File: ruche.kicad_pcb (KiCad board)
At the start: 2 copper layers, 71.8 x 99.9 mm, 92 parts, among them IC1 CN3791, IC2 MAX17048G+, IC3 L86-M33, IC4 SHT41-AD1B-R3, IC5 HX711, J1 Conn_01x02, J13 Micro_SD_Card, J14 Conn_01x03, J15 Conn_01x05, J3 Conn_01x03, J5 Conn_01x04, J6 Conn_01x02, J7 Conn_01x02, J8 Conn_01x03, J9 Conn_01x03, Q1 AO3401A, Q2 MMBT4403, U1 MKRWAN_1310, U2 MS5611-01BA, U3 XC6220B331MR

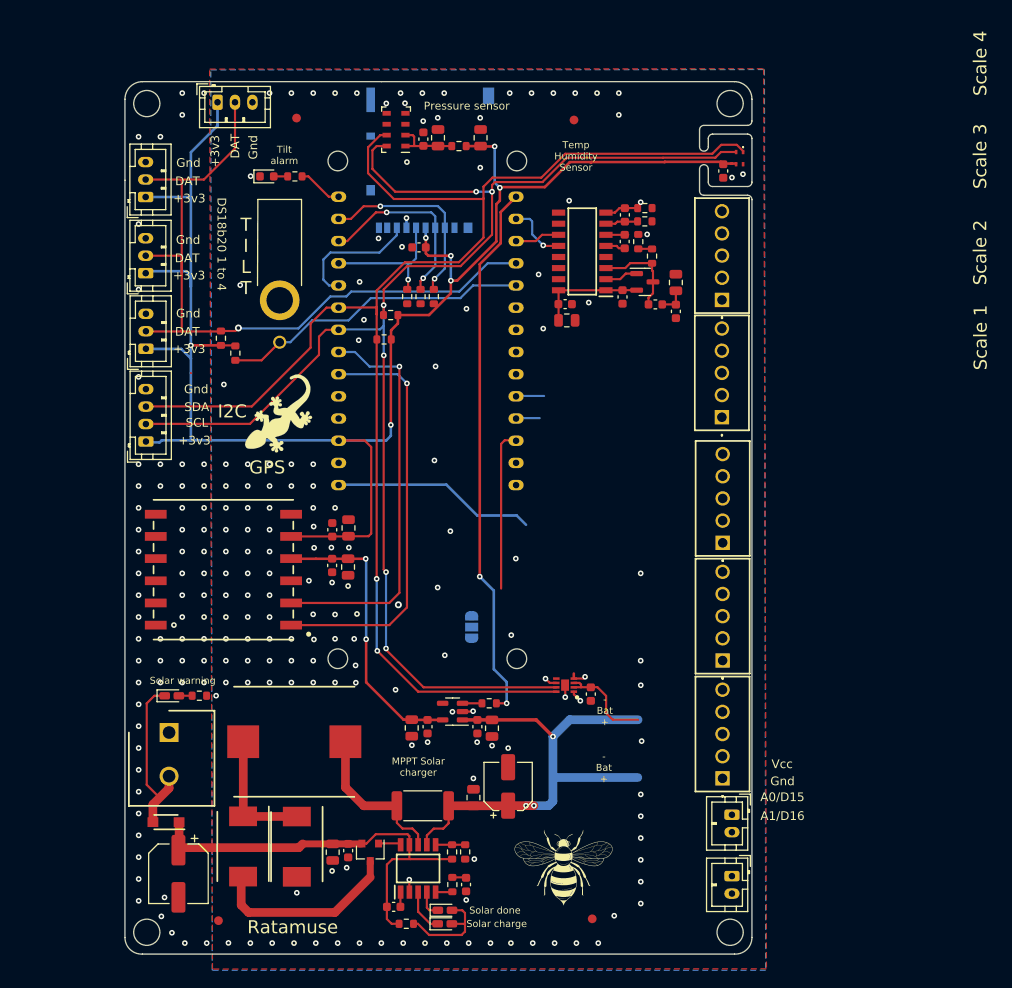
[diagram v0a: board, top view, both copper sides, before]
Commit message: Added HX711
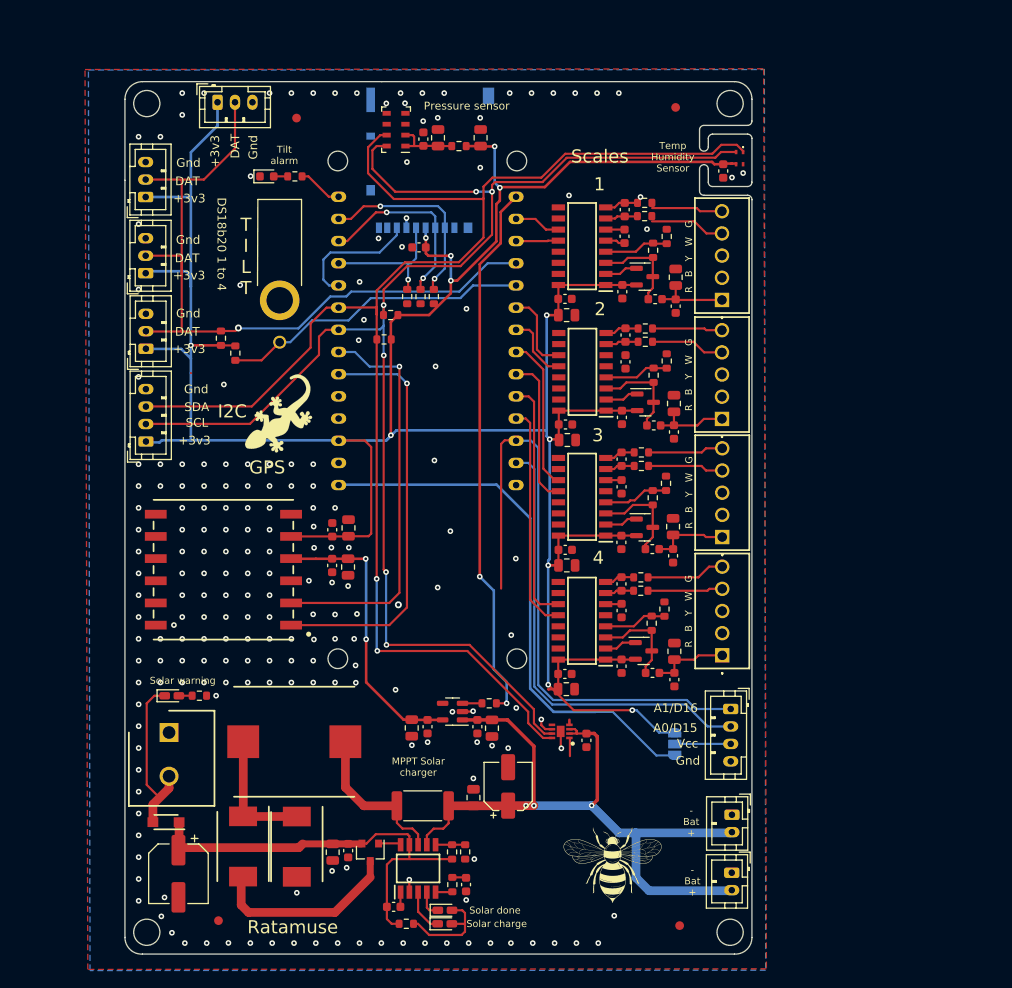
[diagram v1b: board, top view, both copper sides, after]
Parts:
- removed the J15 at (164.9, 148.9)
- removed the J15 at (164.9, 107.5)
- removed the J15 at (164.9, 135.4)
- removed the J15 at (164.9, 121.9)
- added C29: 0.1µF, Capacitor_SMD:C_0603_1608Metric, F.Cu at (159.4, 109.2)
- added C30: 10µF, Capacitor_SMD:C_0805_2012Metric, F.Cu at (159.4, 106.0)
- added C31: 0.1µF, Capacitor_SMD:C_0603_1608Metric, F.Cu at (153.8, 98.1)
- added C32: 0.1µF, Capacitor_SMD:C_0603_1608Metric, F.Cu at (153.8, 101.2)
- added C33: 0.1µF, Capacitor_SMD:C_0603_1608Metric, F.Cu at (153.4, 107.5)
- added C34: 0.1µF, Capacitor_SMD:C_0603_1608Metric, F.Cu at (146.9, 108.4)
- added C35: 10µF, Capacitor_SMD:C_0805_2012Metric, F.Cu at (147.2, 110.1)
- added C36: 0.1µF, Capacitor_SMD:C_0603_1608Metric, F.Cu at (159.3, 123.4)
- added C37: 10µF, Capacitor_SMD:C_0805_2012Metric, F.Cu at (159.3, 120.1)
- added C38: 0.1µF, Capacitor_SMD:C_0603_1608Metric, F.Cu at (153.4, 112.3)
- added C39: 0.1µF, Capacitor_SMD:C_0603_1608Metric, F.Cu at (153.4, 115.5)
- added C40: 0.1µF, Capacitor_SMD:C_0603_1608Metric, F.Cu at (153.3, 121.9)
- added C41: 0.1µF, Capacitor_SMD:C_0603_1608Metric, F.Cu at (146.9, 122.7)
- added C42: 10µF, Capacitor_SMD:C_0805_2012Metric, F.Cu at (147.1, 124.5)
- added C43: 0.1µF, Capacitor_SMD:C_0603_1608Metric, F.Cu at (159.4, 137.6)
- added C44: 10µF, Capacitor_SMD:C_0805_2012Metric, F.Cu at (159.4, 134.3)
- added C45: 0.1µF, Capacitor_SMD:C_0603_1608Metric, F.Cu at (153.4, 126.6)
- added C46: 0.1µF, Capacitor_SMD:C_0603_1608Metric, F.Cu at (153.4, 129.7)
- added C47: 0.1µF, Capacitor_SMD:C_0603_1608Metric, F.Cu at (153.4, 136.0)
- added C48: 0.1µF, Capacitor_SMD:C_0603_1608Metric, F.Cu at (146.9, 136.9)
- added C49: 10µF, Capacitor_SMD:C_0805_2012Metric, F.Cu at (147.0, 138.7)
- added IC6: HX711, Empreintes:SOIC127P600X160-16N, F.Cu at (148.9, 102.3)
- added IC7: HX711, Empreintes:SOIC127P600X160-16N, F.Cu at (148.8, 116.6)
- added IC8: HX711, Empreintes:SOIC127P600X160-16N, F.Cu at (148.8, 130.8)
- added J10: Conn_01x05, Empreintes:connecteurs5, F.Cu at (164.9, 134.8)
- added J16: Conn_01x05, Empreintes:connecteurs5, F.Cu at (164.9, 107.7)
- added J2: Conn_01x05, Empreintes:connecteurs5, F.Cu at (164.9, 121.2)
- added J4: Conn_01x04, Connector_JST:JST_PH_B4B-PH-K_1x04_P2.00mm_Vertical, F.Cu at (165.9, 140.9)
- added L3: 3.3µH, Inductor_SMD:L_0603_1608Metric, F.Cu at (157.1, 108.5)
- added L4: 3.3µH, Inductor_SMD:L_0603_1608Metric, F.Cu at (156.9, 122.6)
- added L5: 3.3µH, Inductor_SMD:L_0603_1608Metric, F.Cu at (156.9, 136.8)
- added Q3: MMBT4403, Package_TO_SOT_SMD:SOT-23, F.Cu at (156.1, 105.8)
- added Q4: MMBT4403, Package_TO_SOT_SMD:SOT-23, F.Cu at (156.0, 120.1)
- added Q5: MMBT4403, Package_TO_SOT_SMD:SOT-23, F.Cu at (155.9, 134.3)
- added R20: 20K, Resistor_SMD:R_0603_1608Metric, F.Cu at (157.0, 102.7)
- added R21: 8.2K, Resistor_SMD:R_0603_1608Metric, F.Cu at (158.5, 101.1)
- added R22: 100, Resistor_SMD:R_0603_1608Metric, F.Cu at (156.1, 98.9)
- added R23: 100, Resistor_SMD:R_0603_1608Metric, F.Cu at (156.1, 97.4)
- added R24: 20K, Resistor_SMD:R_0603_1608Metric, F.Cu at (156.9, 116.8)
- added R25: 8.2K, Resistor_SMD:R_0603_1608Metric, F.Cu at (158.5, 115.1)
- added R26: 100, Resistor_SMD:R_0603_1608Metric, F.Cu at (155.6, 113.1)
- added R27: 100, Resistor_SMD:R_0603_1608Metric, F.Cu at (155.6, 111.6)
- added R28: 20K, Resistor_SMD:R_0603_1608Metric, F.Cu at (156.8, 131.1)
- added R29: 8.2K, Resistor_SMD:R_0603_1608Metric, F.Cu at (158.3, 129.5)
- added R30: 100, Resistor_SMD:R_0603_1608Metric, F.Cu at (155.6, 127.4)
- added R31: 100, Resistor_SMD:R_0603_1608Metric, F.Cu at (155.6, 125.9)
- moved JP1 26.8 mm to (159.5, 145.0)
- moved FID2 11.7 mm to (159.6, 72.0)
- moved FID3 10.0 mm to (160.0, 165.8)
- moved G*** 5.62 mm to (156.1, 158.8)
- moved C5 5.32 mm to (149.3, 144.5)
- moved IC2 5.32 mm to (146.4, 143.5)
- moved R17 3.31 mm to (158.5, 86.8)
- moved R16 0.68 mm to (157.0, 88.4)
- moved IC5 0.60 mm to (148.8, 87.9)
- moved C22 0.60 mm to (159.6, 94.8)
- moved C23 0.60 mm to (159.6, 91.5)
- moved C24 0.60 mm to (153.7, 83.8)
- moved C26 0.60 mm to (146.9, 94.0)
- moved C28 0.60 mm to (153.5, 93.2)
- moved L2 0.60 mm to (157.2, 94.0)
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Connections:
- J15 pad 1: GND -> Net-(C22-Pad1)
- J15 pad 2: Net-(J15-Pad2) -> GND
- J15 pad 3: Net-(J15-Pad3) -> GND
- J15 pad 4: GND -> Net-(J15-Pad4)
- J15 pad 5: Net-(C22-Pad1) -> Net-(J15-Pad5)
- R18 pad 2: Net-(J15-Pad3) -> Net-(J15-Pad4)
- R19 pad 2: Net-(J15-Pad2) -> Net-(J15-Pad5)
- U1 pad 12: CLK1 -> DAT1
- U1 pad 13: DAT1 -> CLK1
- U1 pad 4: CLK2 -> DAT4
- U1 pad 5: DAT2 -> CLK4
- U1 pad 6: CLK3 -> DAT3
- U1 pad 7: DAT3 -> CLK3
- U1 pad 8: CLK4 -> DAT2
- U1 pad 9: DAT4 -> CLK2
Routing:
- net +3V3: track 208.6 -> 328.6 mm, vias 7 -> 12
- net A1/D16: track 18.4 -> 71.6 mm
- net A0/D15: track 0.00 -> 51.7 mm
- net +5V: track 23.4 -> 62.8 mm
- net CLK4: track 0.00 -> 27.9 mm
- net DAT4: track 0.00 -> 26.0 mm
- net CLK3: track 0.00 -> 17.6 mm
- net VBAT: track 68.9 -> 86.3 mm, vias 4 -> 3
- net DAT3: track 0.00 -> 17.2 mm
- net Net-(IC7-Pad3): track 0.00 -> 11.2 mm
- net Net-(IC6-Pad3): track 0.00 -> 11.0 mm
- net Net-(IC8-Pad3): track 0.00 -> 10.8 mm
- net Net-(J10-Pad5): track 0.00 -> 9.00 mm
- net Net-(C36-Pad1): track 0.00 -> 8.94 mm
- net Net-(C43-Pad1): track 0.00 -> 8.92 mm
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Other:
- board text added: "1"
- board text added: "2"
- board text added: "3"
- board text added: "4"
- board text added: "R B Y W G"
- board text added: "Scales"
- board text removed: "Scale 1"
- board text removed: "Scale 2"
- board text removed: "Scale 3"
- board text removed: "Scale 4"

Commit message: design updated
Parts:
- moved C26 7.31 mm to (154.2, 93.9)
- moved C27 7.31 mm to (154.4, 95.8)
- moved C49 7.14 mm to (154.2, 138.3)
- moved C35 7.07 mm to (154.2, 110.0)
- moved C42 6.98 mm to (154.1, 124.1)
- moved C28 5.01 mm to (148.5, 94.0), turned to 0 degrees
- moved FID2 1.87 mm to (158.3, 73.4)
- moved C41 1.68 mm to (148.6, 122.7)
- moved C48 1.65 mm to (148.5, 136.9)
- moved C34 1.50 mm to (148.4, 108.4)
- moved FID3 1.19 mm to (159.0, 165.2)
- moved C33 0.96 mm to (154.0, 108.3), turned to 0 degrees
- moved C47 0.77 mm to (154.0, 136.5), turned to 0 degrees
- moved C40 0.74 mm to (153.9, 122.4), turned to 0 degrees
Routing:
- net +3V3: track 328.6 -> 355.6 mm
- net GND: track 12.8 -> 20.4 mm, vias 203 -> 246
- net VBAT: track 86.3 -> 87.3 mm

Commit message: update
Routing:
- net A1/D16: track 71.6 -> 53.2 mm
- net GND: track 20.4 -> 26.7 mm, vias 246 -> 252
- net Net-(C32-Pad2): track 0.00 -> 2.22 mm
- net VBAT: track 87.3 -> 86.3 mm

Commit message: update
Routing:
- net A1/D16: track 53.2 -> 71.6 mm
- net GND: track 26.7 -> 20.4 mm, vias 252 -> 246
- net Net-(C32-Pad2): track 2.22 -> 0.00 mm
- net VBAT: track 86.3 -> 87.3 mm

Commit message: Update
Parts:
- added C50: 0.1µF, Capacitor_SMD:C_0603_1608Metric, F.Cu at (115.2, 94.6)
- added C51: 10µF, Capacitor_SMD:C_0603_1608Metric, F.Cu at (135.2, 139.8)
- added C52: 0.1µF, Capacitor_SMD:C_0805_2012Metric, F.Cu at (136.9, 140.0)
- added C53: 0.1µF, Capacitor_SMD:C_0603_1608Metric, F.Cu at (129.8, 139.8)
- added C54: 10µF, Capacitor_SMD:C_0805_2012Metric, F.Cu at (128.2, 140.0)
- added G***: LOGO, Empreintes:alvéoles, B.Cu at (154.7, 91.6)
- added J11: Conn_01x04, Connector_JST:JST_PH_B4B-PH-K_1x04_P2.00mm_Vertical, F.Cu at (103.7, 99.7)
- added J12: Conn_01x04, Connector_JST:JST_PH_B4B-PH-K_1x04_P2.00mm_Vertical, F.Cu at (88.8, 110.4)
- added J17: Conn_01x04, Connector_JST:JST_PH_B4B-PH-K_1x04_P2.00mm_Vertical, F.Cu at (88.7, 99.7)
- added J18: Conn_01x04, Connector_JST:JST_PH_B4B-PH-K_1x04_P2.00mm_Vertical, F.Cu at (103.7, 110.4)
- added R32: 10K, Resistor_SMD:R_0603_1608Metric, F.Cu at (108.3, 96.2)
- added R33: 10K, Resistor_SMD:R_0603_1608Metric, F.Cu at (116.6, 109.3)
- added R34: 10K, Resistor_SMD:R_0603_1608Metric, F.Cu at (118.0, 109.3)
- added R35: 10K, Resistor_SMD:R_0603_1608Metric, F.Cu at (113.8, 109.4)
- added R36: 10K, Resistor_SMD:R_0603_1608Metric, F.Cu at (115.2, 109.3)
- added R37: 10K, Resistor_SMD:R_0603_1608Metric, F.Cu at (111.0, 109.4)
- added R38: 10K, Resistor_SMD:R_0603_1608Metric, F.Cu at (112.4, 109.4)
- added R39: 10K, Resistor_SMD:R_0603_1608Metric, F.Cu at (108.3, 109.4)
- added R40: 10K, Resistor_SMD:R_0603_1608Metric, F.Cu at (109.7, 109.4)
- added R41: 10K, Resistor_SMD:R_0603_1608Metric, F.Cu at (136.0, 137.1)
- added U4: TCA9548APWR, Package_SO:TSSOP-24_4.4x7.8mm_P0.65mm, F.Cu at (113.6, 100.2)
- added U5: XC6220B331MR, Package_TO_SOT_SMD:SOT-23-5, F.Cu at (132.5, 138.1)
- J4: value Conn_01x04 -> Conn_01x03; footprint Connector_JST:JST_PH_B4B-PH-K_1x04_P2.00mm_Vertical -> Connector_JST:JST_PH_B3B-PH-K_1x03_P2.00mm_Vertical
- moved J5 62.1 mm to (147.9, 72.2), turned to 0 degrees
- moved G*** 53.7 mm to (149.4, 112.7)
- moved G*** 24.1 mm to (113.1, 131.6)
- moved G*** 20.1 mm to (97.8, 122.2)
- moved FID4 15.3 mm to (92.2, 162.0)
- moved R10 14.8 mm to (123.7, 102.9), turned to 90 degrees
- moved FID1 11.8 mm to (104.4, 72.2)
- moved J3 11.7 mm to (103.8, 89.0)
- moved R7 11.4 mm to (125.3, 107.1), turned to 180 degrees
- moved R9 10.8 mm to (108.0, 87.7)
- moved IC3 10.5 mm to (89.6, 119.9)
- moved C11 10.5 mm to (111.6, 124.7)
- moved C20 10.5 mm to (109.8, 120.4)
- moved C21 10.5 mm to (111.6, 120.2)
- moved C6 10.5 mm to (109.8, 124.5)
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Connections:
- C10 pad 1: +3V3 -> VCC
- C12 pad 1: +3V3 -> VCC
- C19 pad 1: +3V3 -> VCC
- C26 pad 1: +3V3 -> VCC
- C27 pad 1: +3V3 -> VCC
- C28 pad 1: +3V3 -> VCC
- C33 pad 1: +3V3 -> VCC
- C34 pad 1: +3V3 -> VCC
- C35 pad 1: +3V3 -> VCC
- C40 pad 1: +3V3 -> VCC
- C41 pad 1: +3V3 -> VCC
- C42 pad 1: +3V3 -> VCC
- C47 pad 1: +3V3 -> VCC
- C48 pad 1: +3V3 -> VCC
- C49 pad 1: +3V3 -> VCC
- FB1 pad 2: +3V3 -> VCC
- IC4 pad 3: +3V3 -> VCC
- IC5 pad 1: +3V3 -> VCC
- IC5 pad 16: +3V3 -> VCC
- IC6 pad 1: +3V3 -> VCC
- IC6 pad 16: +3V3 -> VCC
- IC7 pad 1: +3V3 -> VCC
- IC7 pad 16: +3V3 -> VCC
- IC8 pad 1: +3V3 -> VCC
- IC8 pad 16: +3V3 -> VCC
- J13 pad 4: +3V3 -> VCC
- J14 pad 1: +3V3 -> VCC
- J3 pad 1: +3V3 -> VCC
- J4 pad 1: A1/D16 -> A0/D15
- J4 pad 2: A0/D15 -> Net-(JP1-Pad2)
- J4 pad 3: Net-(J4-Pad3) -> GND
- J5 pad 1: +3V3 -> VCC
- J8 pad 1: +3V3 -> VCC
- J9 pad 1: +3V3 -> VCC
- JP1 pad 2: Net-(J4-Pad3) -> Net-(JP1-Pad2)
- Q2 pad 2: +3V3 -> VCC
- Q3 pad 2: +3V3 -> VCC
- Q4 pad 2: +3V3 -> VCC
- Q5 pad 2: +3V3 -> VCC
- R13 pad 1: +3V3 -> VCC
- R14 pad 1: +3V3 -> VCC
- R15 pad 1: +3V3 -> VCC
- R9 pad 2: +3V3 -> VCC
- U1 pad 3: A1/D16 -> Start_modules
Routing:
- net VCC: track 0.00 -> 412.2 mm, vias 0 -> 13
- net +3V3: track 355.6 -> 91.4 mm, vias 12 -> 3
- net A1/D16: track 71.6 -> 0.00 mm
- net SD3: track 0.00 -> 38.2 mm
- net SC3: track 0.00 -> 37.8 mm
- net SD1: track 0.00 -> 35.3 mm
- net SC1: track 0.00 -> 33.3 mm
- net Start_modules: track 0.00 -> 31.3 mm, vias 0 -> 2
- net SC2: track 0.00 -> 20.7 mm
- net SD0: track 0.00 -> 20.5 mm
- net SD2: track 0.00 -> 19.9 mm
- net SC0: track 0.00 -> 19.0 mm
- net VBAT: track 87.3 -> 104.4 mm
- net RX_GPS: track 48.0 -> 58.5 mm
- net TX_GPS: track 46.4 -> 56.9 mm
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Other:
- board size 71.8 x 99.9 mm -> 82.8 x 99.9 mm
- board text added: "1-DAT-2"
- board text added: "3-DAT-4"
- board text added: "SHT40-1"
- board text added: "SHT40-2"
- board text added: "SHT40-3"
- board text added: "SHT40-4"
- board text removed: "A1/D16"
- board text removed: "DAT"

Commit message: Ajouté code
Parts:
- removed R12, R41: 10K, Resistor_SMD:R_0603_1608Metric
- added J19: Conn_01x02, Connector_JST:JST_PH_B2B-PH-K_1x02_P2.00mm_Vertical, F.Cu at (114.1, 114.4)
- C21: value 10µF -> 4.7µF
- moved R39 0.11 mm to (108.3, 109.3)
- moved R40 0.10 mm to (109.7, 109.3)
- moved R37 0.09 mm to (111.0, 109.3)
- moved R38 0.07 mm to (112.4, 109.3)
- moved R34 0.07 mm to (117.9, 109.3)
- moved R35 0.06 mm to (113.8, 109.3)
- moved R33 0.05 mm to (116.5, 109.3)
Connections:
- U1 pad 24: unconnected-(U1-Pad24) -> Reset-button
- U3 pad 3: Net-(R12-Pad1) -> Start_GPS
- U5 pad 3: Net-(R41-Pad1) -> Start_modules
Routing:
- net Reset-button: track 0.00 -> 13.4 mm
- net Start_GPS: track 52.4 -> 56.3 mm
- net Start_modules: track 31.3 -> 33.8 mm
- net Net-(R12-Pad1): track 2.23 -> 0.00 mm
- net Net-(R41-Pad1): track 1.48 -> 0.00 mm
- net CLK3: track 16.9 -> 17.9 mm
- net DAT3: track 15.7 -> 16.5 mm
- net GND: vias 282 -> 284
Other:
- board text added: "Opensource connected hive V0.2 by Ratamuse"
- board text added: "Reset"
- board text removed: "Open beehive scale board V0.2 by Ratamuse"
